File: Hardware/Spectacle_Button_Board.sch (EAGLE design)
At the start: 50 parts, among them J17 AUDIO-JACK3, J19 FTDI_DEVICE, J20 AUDIO-JACK3, U1 CY8C4146LQI-S422, U2 3.3V/150mA

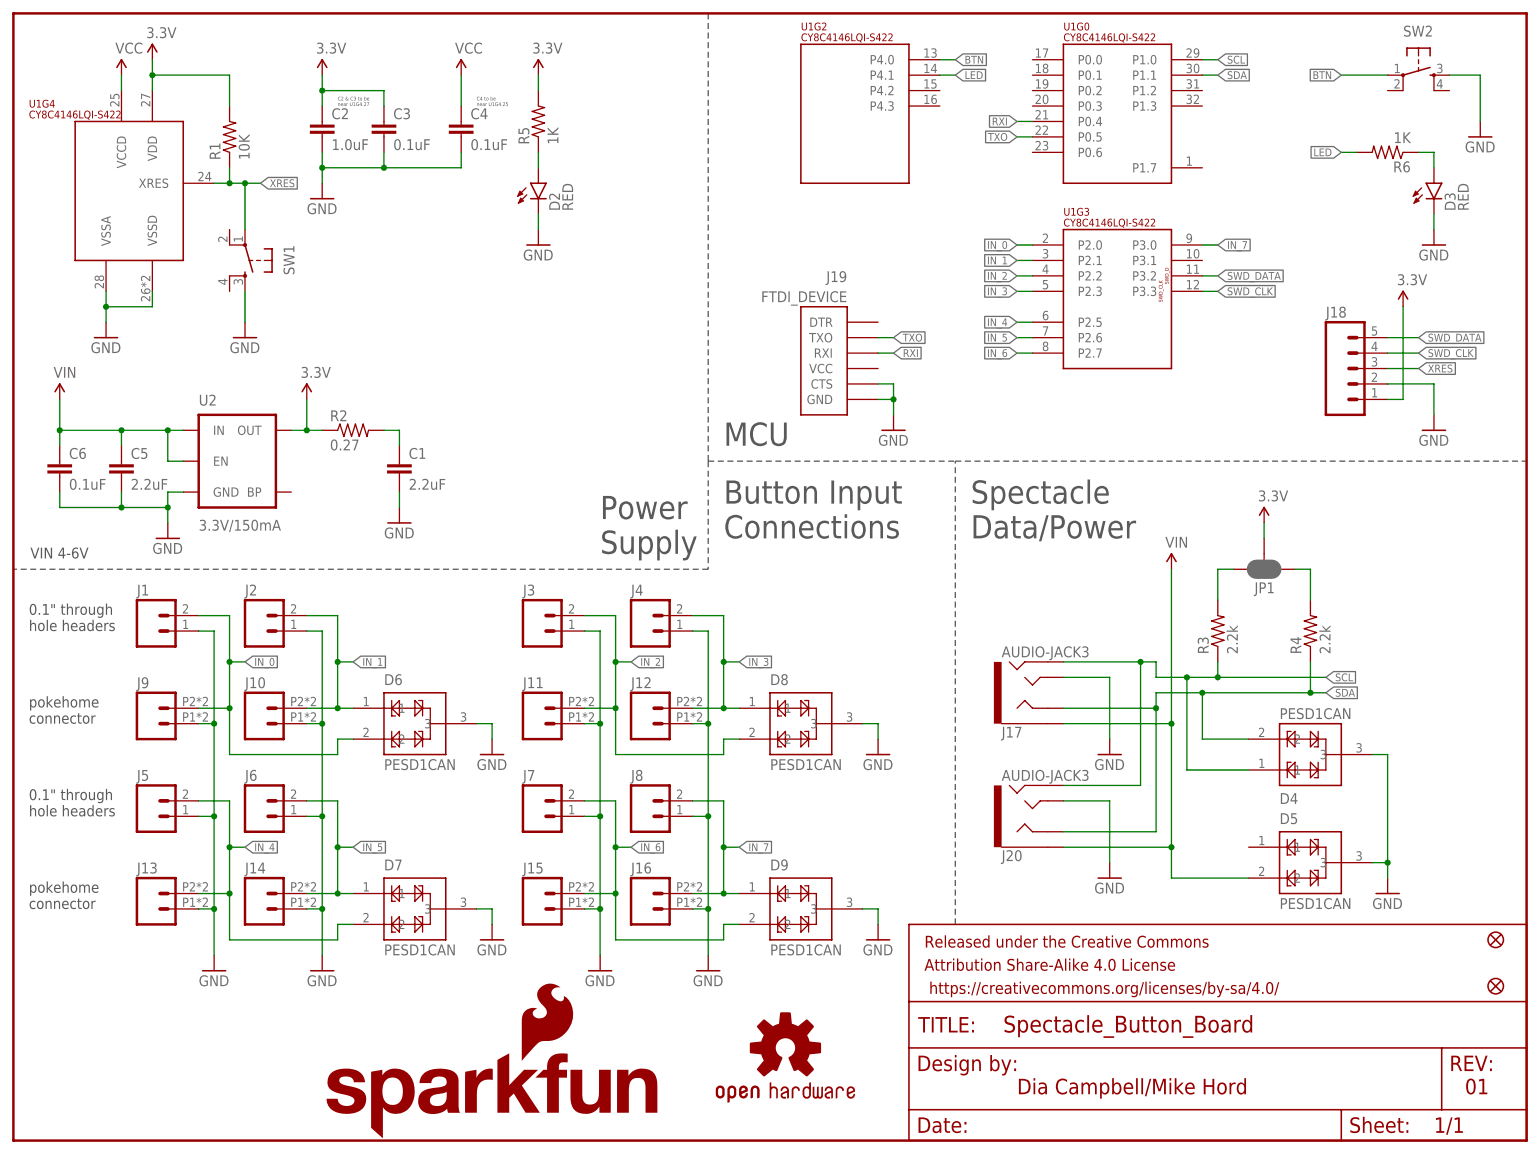
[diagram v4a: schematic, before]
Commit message: Added circuitry for downstream power control
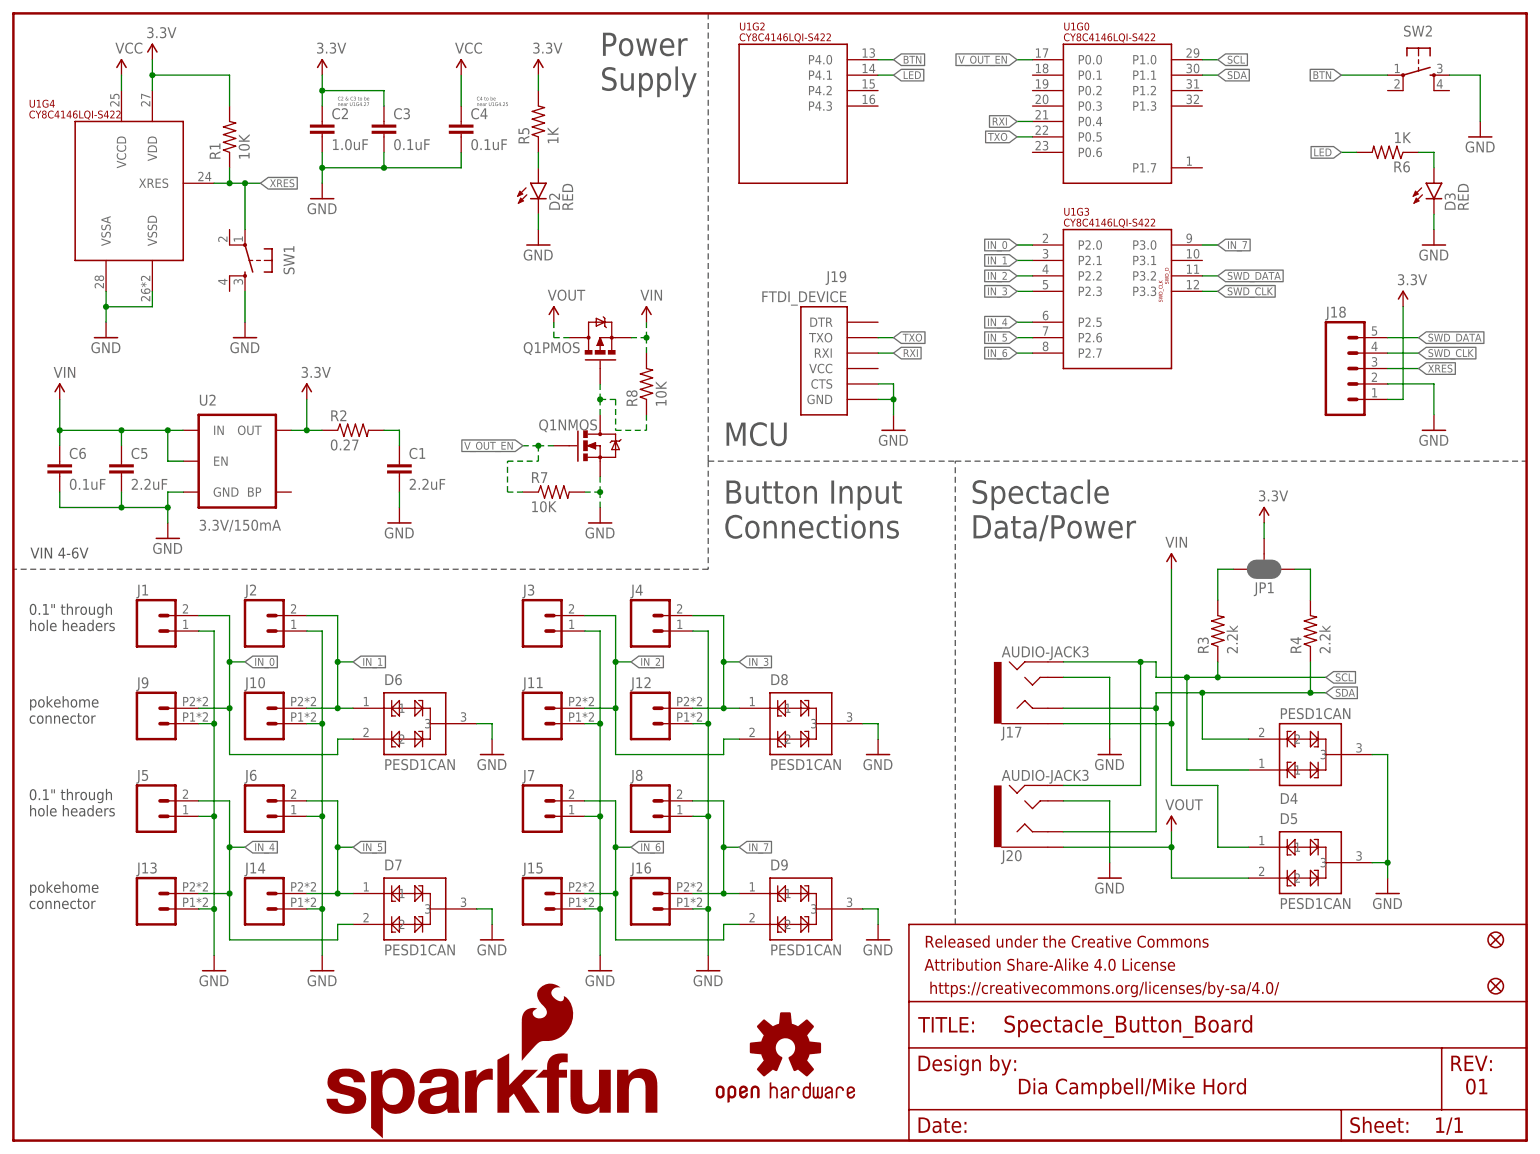
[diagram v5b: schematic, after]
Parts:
- added Q1: (no value), SparkFun-DiscreteSemi:IRF7509
- added R7, R8: 10K, SparkFun-Resistors:10KOHM-1/10W-1%(0603)0603
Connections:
- new net N$26: Q1NMOS.D, Q1PMOS.G, R8.1
- new net VOUT: D5.2, J20.EARTH, Q1PMOS.D
- new net V_OUT_EN: Q1NMOS.G, R7.1, U1G0.P0.0
- net GND: now also Q1NMOS.S, R7.2
- net VIN: now also D5.1, Q1PMOS.S, R8.2; no longer D5.2, J20.EARTH
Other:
- moved on the sheet: U1G2
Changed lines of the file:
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@@
 <layer number="255" name="routoute" color="7" fill="1" visible="yes" active="yes"/>
 </layers>
-<schematic xreflabel="%F%N/%S" xrefpart="/%S.%C%R">
+<schematic xreflabel="%F%N/%S" xrefpart="1_/%S.%C%R">
 <attributes>
 </attributes>
@@
 <part name="FD1" library="SparkFun-Aesthetics" deviceset="FIDUCIAL" device="UFIDUCIAL"/>
 <part name="FD2" library="SparkFun-Aesthetics" deviceset="FIDUCIAL" device="UFIDUCIAL"/>
+<part name="Q1" library="SparkFun-DiscreteSemi" deviceset="IRF7509" device=""/>
+<part name="GND22" library="SparkFun-Aesthetics" deviceset="GND" device=""/>
+<part name="SUPPLY15" library="SparkFun-Aesthetics" deviceset="VIN" device=""/>
+<part name="U$4" library="SparkFun-Aesthetics" deviceset="VOUT" device=""/>
+<part name="R7" library="SparkFun-Resistors" deviceset="10KOHM-1/10W-1%(0603)" device="0603" value="10K"/>
+<part name="R8" library="SparkFun-Resistors" deviceset="10KOHM-1/10W-1%(0603)" device="0603" value="10K"/>
+<part name="U$1" library="SparkFun-Aesthetics" deviceset="VOUT" device=""/>
 </parts>
 <sheets>
@@
 Data/Power</text>
 <text x="116.84" y="114.3" size="3.81" layer="97">MCU</text>
-<text x="96.52" y="96.52" size="3.81" layer="97">Power
+<text x="96.52" y="172.72" size="3.81" layer="97">Power
 Supply</text>
 <text x="165.1" y="7.62" size="2.54" layer="94">Dia Campbell/Mike Hord</text>
@@
 <instance part="FRAME1" gate="G$1" x="0" y="0"/>
 <instance part="FRAME1" gate="V" x="147.32" y="0"/>
-<instance part="U1" gate="G2" x="129.54" y="157.48"/>
+<instance part="U1" gate="G2" x="119.38" y="157.48"/>
 <instance part="U1" gate="G0" x="172.72" y="157.48"/>
 <instance part="U1" gate="G3" x="172.72" y="127"/>
@@
 <instance part="FD1" gate="G$1" x="243.84" y="33.02"/>
 <instance part="FD2" gate="G$1" x="243.84" y="25.4"/>
+<instance part="Q1" gate="NMOS" x="96.52" y="114.3" smashed="yes">
+<attribute name="NAME" x="86.36" y="116.84" size="1.778" layer="95"/>
+<attribute name="VALUE" x="101.6" y="114.3" size="1.778" layer="96"/>
+</instance>
+<instance part="Q1" gate="PMOS" x="96.52" y="132.08" smashed="yes" rot="R90">
+<attribute name="NAME" x="83.82" y="129.54" size="1.778" layer="95"/>
+<attribute name="VALUE" x="96.52" y="137.16" size="1.778" layer="96" rot="R90"/>
+</instance>
+<instance part="GND22" gate="1" x="96.52" y="101.6"/>
+<instance part="SUPPLY15" gate="G$1" x="104.14" y="134.62"/>
+<instance part="U$4" gate="G$1" x="88.9" y="134.62"/>
+<instance part="R7" gate="G$1" x="88.9" y="106.68"/>
+<instance part="R8" gate="G$1" x="104.14" y="124.46" rot="R90"/>
+<instance part="U$1" gate="G$1" x="190.5" y="50.8"/>
 </instances>
 <busses>
@@
 <wire x1="180.34" y1="55.88" x2="180.34" y2="45.72" width="0.1524" layer="91"/>
 </segment>
+<segment>
+<pinref part="Q1" gate="NMOS" pin="S"/>
+<pinref part="GND22" gate="1" pin="GND"/>
+<wire x1="96.52" y1="109.22" x2="96.52" y2="106.68" width="0.1524" layer="91" style="longdash"/>
+<pinref part="R7" gate="G$1" pin="2"/>
+<wire x1="96.52" y1="106.68" x2="96.52" y2="104.14" width="0.1524" layer="91" style="longdash"/>
+<wire x1="93.98" y1="106.68" x2="96.52" y2="106.68" width="0.1524" layer="91" style="longdash"/>
+<junction x="96.52" y="106.68"/>
+</segment>
 </net>
 <net name="IN_0" class="0">
@@
 </segment>
 <segment>
-<pinref part="D5" gate="G$1" pin="2"/>
 <pinref part="SUPPLY7" gate="G$1" pin="VIN"/>
-<wire x1="203.2" y1="43.18" x2="190.5" y2="43.18" width="0.1524" layer="91"/>
-<wire x1="190.5" y1="43.18" x2="190.5" y2="48.26" width="0.1524" layer="91"/>
-<pinref part="J20" gate="G$1" pin="EARTH"/>
-<wire x1="190.5" y1="48.26" x2="190.5" y2="68.58" width="0.1524" layer="91"/>
 <wire x1="190.5" y1="68.58" x2="190.5" y2="93.98" width="0.1524" layer="91"/>
-<wire x1="172.72" y1="48.26" x2="190.5" y2="48.26" width="0.1524" layer="91"/>
-<junction x="190.5" y="48.26"/>
 <pinref part="J17" gate="G$1" pin="EARTH"/>
 <wire x1="172.72" y1="68.58" x2="190.5" y2="68.58" width="0.1524" layer="91"/>
+<pinref part="D5" gate="G$1" pin="1"/>
+<wire x1="203.2" y1="48.26" x2="198.12" y2="48.26" width="0.1524" layer="91"/>
+<wire x1="198.12" y1="48.26" x2="198.12" y2="58.42" width="0.1524" layer="91"/>
+<wire x1="198.12" y1="58.42" x2="190.5" y2="58.42" width="0.1524" layer="91"/>
+<wire x1="190.5" y1="58.42" x2="190.5" y2="68.58" width="0.1524" layer="91"/>
 <junction x="190.5" y="68.58"/>
+</segment>
+<segment>
+<pinref part="Q1" gate="PMOS" pin="S"/>
+<wire x1="101.6" y1="132.08" x2="104.14" y2="132.08" width="0.1524" layer="91" style="longdash"/>
+<wire x1="104.14" y1="132.08" x2="104.14" y2="134.62" width="0.1524" layer="91" style="longdash"/>
+<pinref part="SUPPLY15" gate="G$1" pin="VIN"/>
+<pinref part="R8" gate="G$1" pin="2"/>
+<wire x1="104.14" y1="129.54" x2="104.14" y2="132.08" width="0.1524" layer="91" style="longdash"/>
+<junction x="104.14" y="132.08"/>
 </segment>
 </net>
@@
 <segment>
 <pinref part="U1" gate="G2" pin="P4.0"/>
-<wire x1="152.4" y1="177.8" x2="154.94" y2="177.8" width="0.1524" layer="91"/>
-<label x="154.94" y="177.8" size="1.27" layer="95" xref="yes"/>
+<wire x1="142.24" y1="177.8" x2="144.78" y2="177.8" width="0.1524" layer="91"/>
+<label x="144.78" y="177.8" size="1.27" layer="95" xref="yes"/>
 </segment>
 <segment>
@@
 <segment>
 <pinref part="U1" gate="G2" pin="P4.1"/>
-<wire x1="152.4" y1="175.26" x2="154.94" y2="175.26" width="0.1524" layer="91"/>
-<label x="154.94" y="175.26" size="1.27" layer="95" xref="yes"/>
+<wire x1="142.24" y1="175.26" x2="144.78" y2="175.26" width="0.1524" layer="91"/>
+<label x="144.78" y="175.26" size="1.27" layer="95" xref="yes"/>
 </segment>
 <segment>
@@
 </segment>
 </net>
+<net name="N$26" class="0">
+<segment>
+<pinref part="Q1" gate="PMOS" pin="G"/>
+<pinref part="Q1" gate="NMOS" pin="D"/>
+<wire x1="96.52" y1="124.46" x2="96.52" y2="121.92" width="0.1524" layer="91" style="longdash"/>
+<wire x1="96.52" y1="121.92" x2="96.52" y2="119.38" width="0.1524" layer="91" style="longdash"/>
+<wire x1="96.52" y1="121.92" x2="99.06" y2="121.92" width="0.1524" layer="91" style="longdash"/>
+<junction x="96.52" y="121.92"/>
+<wire x1="99.06" y1="121.92" x2="99.06" y2="116.84" width="0.1524" layer="91" style="longdash"/>
+<pinref part="R8" gate="G$1" pin="1"/>
+<wire x1="99.06" y1="116.84" x2="104.14" y2="116.84" width="0.1524" layer="91" style="longdash"/>
+<wire x1="104.14" y1="116.84" x2="104.14" y2="119.38" width="0.1524" layer="91" style="longdash"/>
+</segment>
+</net>
+<net name="VOUT" class="0">
+<segment>
+<pinref part="Q1" gate="PMOS" pin="D"/>
+<wire x1="91.44" y1="132.08" x2="88.9" y2="132.08" width="0.1524" layer="91" style="longdash"/>
+<wire x1="88.9" y1="132.08" x2="88.9" y2="134.62" width="0.1524" layer="91" style="longdash"/>
+<pinref part="U$4" gate="G$1" pin="VOUT"/>
+</segment>
+<segment>
+<pinref part="D5" gate="G$1" pin="2"/>
+<wire x1="203.2" y1="43.18" x2="190.5" y2="43.18" width="0.1524" layer="91"/>
+<wire x1="190.5" y1="43.18" x2="190.5" y2="48.26" width="0.1524" layer="91"/>
+<pinref part="J20" gate="G$1" pin="EARTH"/>
+<wire x1="172.72" y1="48.26" x2="190.5" y2="48.26" width="0.1524" layer="91"/>
+<pinref part="U$1" gate="G$1" pin="VOUT"/>
+<wire x1="190.5" y1="50.8" x2="190.5" y2="48.26" width="0.1524" layer="91"/>
+<junction x="190.5" y="48.26"/>
+</segment>
+</net>
+<net name="V_OUT_EN" class="0">
+<segment>
+<pinref part="Q1" gate="NMOS" pin="G"/>
+<wire x1="88.9" y1="114.3" x2="86.36" y2="114.3" width="0.1524" layer="91" style="longdash"/>
+<label x="83.82" y="114.3" size="1.27" layer="95" rot="R180" xref="yes"/>
+<pinref part="R7" gate="G$1" pin="1"/>
+<wire x1="86.36" y1="114.3" x2="83.82" y2="114.3" width="0.1524" layer="91" style="longdash"/>
+<wire x1="83.82" y1="106.68" x2="81.28" y2="106.68" width="0.1524" layer="91" style="longdash"/>
+<wire x1="81.28" y1="106.68" x2="81.28" y2="111.76" width="0.1524" layer="91" style="longdash"/>
+<wire x1="81.28" y1="111.76" x2="86.36" y2="111.76" width="0.1524" layer="91" style="longdash"/>
+<wire x1="86.36" y1="111.76" x2="86.36" y2="114.3" width="0.1524" layer="91" style="longdash"/>
+<junction x="86.36" y="114.3"/>
+</segment>
+<segment>
+<pinref part="U1" gate="G0" pin="P0.0"/>
+<wire x1="167.64" y1="177.8" x2="165.1" y2="177.8" width="0.1524" layer="91"/>
+<label x="165.1" y="177.8" size="1.27" layer="95" rot="R180" xref="yes"/>
+</segment>
+</net>
